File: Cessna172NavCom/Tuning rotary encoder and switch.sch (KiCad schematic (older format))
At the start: 7 parts, among them J3 EN11-HSM1BF20

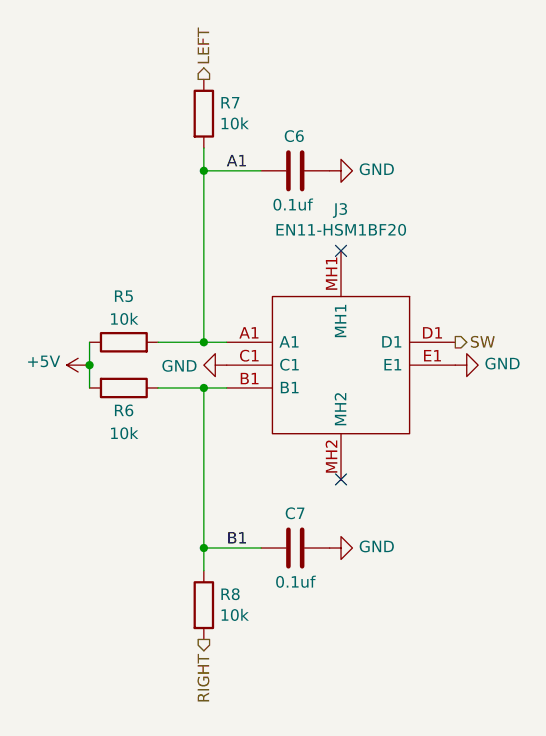
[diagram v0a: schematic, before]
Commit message: Fix courtyard overlap for routing
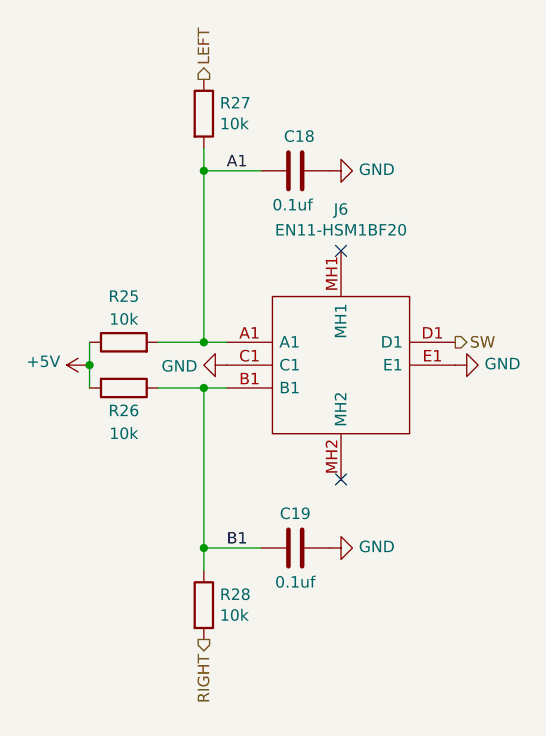
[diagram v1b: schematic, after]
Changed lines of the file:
@@
 $Descr A4 11693 8268
 encoding utf-8
-Sheet 5 15
+Sheet 14 15
 Title ""
 Date ""
@@
 AR Path="/5F71BCEB/5F5D9328" Ref="R25"  Part="1"
 AR Path="/5F71BCF7/5F5D9328" Ref="R29"  Part="1"
-F 0 "R5" V 5450 3850 50  0000 C CNN
+F 0 "R25" V 5450 3850 50  0000 C CNN
 F 1 "10k" V 5350 3850 50  0000 C CNN
 F 2 "Resistor_SMD:R_0805_2012Metric_Pad1.15x1.40mm_HandSolder" V 5180 3850 50  0001 C CNN
@@
 AR Path="/5F71BCEB/5F5D932E" Ref="R26"  Part="1"
 AR Path="/5F71BCF7/5F5D932E" Ref="R30"  Part="1"
-F 0 "R6" V 5350 4050 50  0000 C CNN
+F 0 "R26" V 5350 4050 50  0000 C CNN
 F 1 "10k" V 5450 4050 50  0000 C CNN
 F 2 "Resistor_SMD:R_0805_2012Metric_Pad1.15x1.40mm_HandSolder" V 5180 4050 50  0001 C CNN
@@
 AR Path="/5F71BCEB/5F5D9337" Ref="C19"  Part="1"
 AR Path="/5F71BCF7/5F5D9337" Ref="C21"  Part="1"
-F 0 "C7" V 6150 4750 50  0000 C CNN
+F 0 "C19" V 6150 4750 50  0000 C CNN
 F 1 "0.1uf" V 5850 4750 50  0000 C CNN
 F 2 "Capacitor_SMD:C_0805_2012Metric_Pad1.15x1.40mm_HandSolder" H 6038 4600 50  0001 C CNN
@@
 AR Path="/5F71BCEB/5F5D933D" Ref="C18"  Part="1"
 AR Path="/5F71BCF7/5F5D933D" Ref="C20"  Part="1"
-F 0 "C6" V 5850 3050 50  0000 L CNN
+F 0 "C18" V 5850 3050 50  0000 L CNN
 F 1 "0.1uf" V 6150 3000 50  0000 L CNN
 F 2 "Capacitor_SMD:C_0805_2012Metric_Pad1.15x1.40mm_HandSolder" H 6038 2950 50  0001 C CNN
@@
 AR Path="/5F71BCEB/5F5D934C" Ref="R28"  Part="1"
 AR Path="/5F71BCF7/5F5D934C" Ref="R32"  Part="1"
-F 0 "R8" H 5670 5046 50  0000 L CNN
+F 0 "R28" H 5670 5046 50  0000 L CNN
 F 1 "10k" H 5670 4955 50  0000 L CNN
 F 2 "Resistor_SMD:R_0805_2012Metric_Pad1.15x1.40mm_HandSolder" V 5530 5000 50  0001 C CNN
@@
 AR Path="/5F71BCEB/5F5D935D" Ref="R27"  Part="1"
 AR Path="/5F71BCF7/5F5D935D" Ref="R31"  Part="1"
-F 0 "R7" H 5670 2896 50  0000 L CNN
+F 0 "R27" H 5670 2896 50  0000 L CNN
 F 1 "10k" H 5670 2805 50  0000 L CNN
 F 2 "Resistor_SMD:R_0805_2012Metric_Pad1.15x1.40mm_HandSolder" V 5530 2850 50  0001 C CNN
@@
 AR Path="/5F71BCEB/5F66C873" Ref="J6"  Part="1"
 AR Path="/5F71BCF7/5F66C873" Ref="J7"  Part="1"
-F 0 "J3" V 6019 3450 50  0000 C CNN
+F 0 "J6" V 6019 3450 50  0000 C CNN
 F 1 "EN11-HSM1BF20" V 6110 3450 50  0000 C CNN
 F 2 "SamacSys_Parts:EN11HSM1BF20" H 7050 3750 50  0001 L CNN

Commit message: Fully routed!!!
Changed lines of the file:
@@
 $Descr A4 11693 8268
 encoding utf-8
-Sheet 14 15
+Sheet 15 15
 Title ""
 Date ""
@@
 AR Path="/5F71BCEB/5F5D9328" Ref="R25"  Part="1"
 AR Path="/5F71BCF7/5F5D9328" Ref="R29"  Part="1"
-F 0 "R25" V 5450 3850 50  0000 C CNN
+F 0 "R29" V 5450 3850 50  0000 C CNN
 F 1 "10k" V 5350 3850 50  0000 C CNN
 F 2 "Resistor_SMD:R_0805_2012Metric_Pad1.15x1.40mm_HandSolder" V 5180 3850 50  0001 C CNN
@@
 AR Path="/5F71BCEB/5F5D932E" Ref="R26"  Part="1"
 AR Path="/5F71BCF7/5F5D932E" Ref="R30"  Part="1"
-F 0 "R26" V 5350 4050 50  0000 C CNN
+F 0 "R30" V 5350 4050 50  0000 C CNN
 F 1 "10k" V 5450 4050 50  0000 C CNN
 F 2 "Resistor_SMD:R_0805_2012Metric_Pad1.15x1.40mm_HandSolder" V 5180 4050 50  0001 C CNN
@@
 AR Path="/5F71BCEB/5F5D9337" Ref="C19"  Part="1"
 AR Path="/5F71BCF7/5F5D9337" Ref="C21"  Part="1"
-F 0 "C19" V 6150 4750 50  0000 C CNN
+F 0 "C21" V 6150 4750 50  0000 C CNN
 F 1 "0.1uf" V 5850 4750 50  0000 C CNN
 F 2 "Capacitor_SMD:C_0805_2012Metric_Pad1.15x1.40mm_HandSolder" H 6038 4600 50  0001 C CNN
@@
 AR Path="/5F71BCEB/5F5D933D" Ref="C18"  Part="1"
 AR Path="/5F71BCF7/5F5D933D" Ref="C20"  Part="1"
-F 0 "C18" V 5850 3050 50  0000 L CNN
+F 0 "C20" V 5850 3050 50  0000 L CNN
 F 1 "0.1uf" V 6150 3000 50  0000 L CNN
 F 2 "Capacitor_SMD:C_0805_2012Metric_Pad1.15x1.40mm_HandSolder" H 6038 2950 50  0001 C CNN
@@
 AR Path="/5F71BCEB/5F5D934C" Ref="R28"  Part="1"
 AR Path="/5F71BCF7/5F5D934C" Ref="R32"  Part="1"
-F 0 "R28" H 5670 5046 50  0000 L CNN
+F 0 "R32" H 5670 5046 50  0000 L CNN
 F 1 "10k" H 5670 4955 50  0000 L CNN
 F 2 "Resistor_SMD:R_0805_2012Metric_Pad1.15x1.40mm_HandSolder" V 5530 5000 50  0001 C CNN
@@
 AR Path="/5F71BCEB/5F5D935D" Ref="R27"  Part="1"
 AR Path="/5F71BCF7/5F5D935D" Ref="R31"  Part="1"
-F 0 "R27" H 5670 2896 50  0000 L CNN
+F 0 "R31" H 5670 2896 50  0000 L CNN
 F 1 "10k" H 5670 2805 50  0000 L CNN
 F 2 "Resistor_SMD:R_0805_2012Metric_Pad1.15x1.40mm_HandSolder" V 5530 2850 50  0001 C CNN
@@
 AR Path="/5F71BCEB/5F66C873" Ref="J6"  Part="1"
 AR Path="/5F71BCF7/5F66C873" Ref="J7"  Part="1"
-F 0 "J6" V 6019 3450 50  0000 C CNN
+F 0 "J7" V 6019 3450 50  0000 C CNN
 F 1 "EN11-HSM1BF20" V 6110 3450 50  0000 C CNN
 F 2 "SamacSys_Parts:EN11HSM1BF20" H 7050 3750 50  0001 L CNN

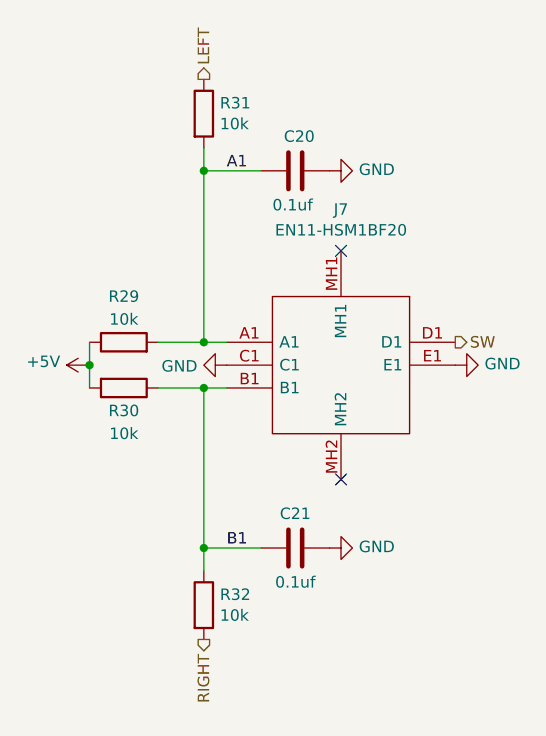
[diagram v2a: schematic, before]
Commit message: Remove unnecessary items, rename some of the nets
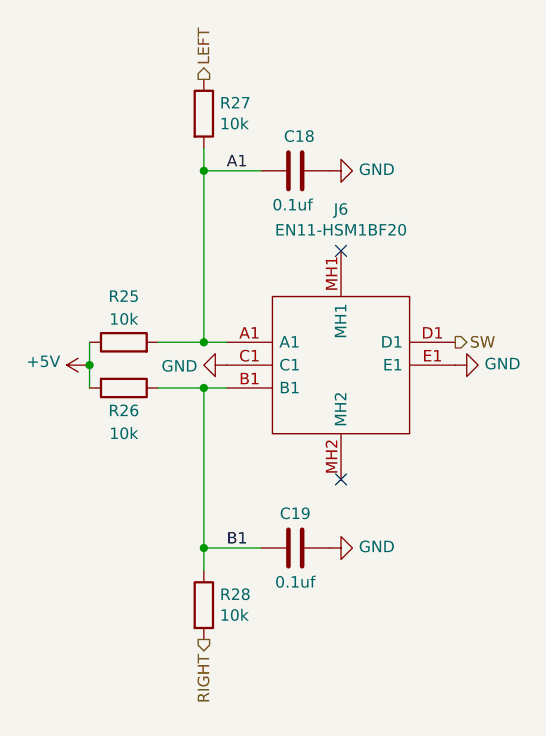
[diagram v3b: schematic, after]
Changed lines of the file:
@@
 $Descr A4 11693 8268
 encoding utf-8
-Sheet 15 15
+Sheet 13 13
 Title ""
 Date ""
@@
 AR Path="/5F71BCEB/5F5D9328" Ref="R25"  Part="1"
 AR Path="/5F71BCF7/5F5D9328" Ref="R29"  Part="1"
-F 0 "R29" V 5450 3850 50  0000 C CNN
+F 0 "R25" V 5450 3850 50  0000 C CNN
 F 1 "10k" V 5350 3850 50  0000 C CNN
 F 2 "Resistor_SMD:R_0805_2012Metric_Pad1.15x1.40mm_HandSolder" V 5180 3850 50  0001 C CNN
@@
 AR Path="/5F71BCEB/5F5D932E" Ref="R26"  Part="1"
 AR Path="/5F71BCF7/5F5D932E" Ref="R30"  Part="1"
-F 0 "R30" V 5350 4050 50  0000 C CNN
+F 0 "R26" V 5350 4050 50  0000 C CNN
 F 1 "10k" V 5450 4050 50  0000 C CNN
 F 2 "Resistor_SMD:R_0805_2012Metric_Pad1.15x1.40mm_HandSolder" V 5180 4050 50  0001 C CNN
@@
 AR Path="/5F71BCEB/5F5D9337" Ref="C19"  Part="1"
 AR Path="/5F71BCF7/5F5D9337" Ref="C21"  Part="1"
-F 0 "C21" V 6150 4750 50  0000 C CNN
+F 0 "C19" V 6150 4750 50  0000 C CNN
 F 1 "0.1uf" V 5850 4750 50  0000 C CNN
 F 2 "Capacitor_SMD:C_0805_2012Metric_Pad1.15x1.40mm_HandSolder" H 6038 4600 50  0001 C CNN
@@
 AR Path="/5F71BCEB/5F5D933D" Ref="C18"  Part="1"
 AR Path="/5F71BCF7/5F5D933D" Ref="C20"  Part="1"
-F 0 "C20" V 5850 3050 50  0000 L CNN
+F 0 "C18" V 5850 3050 50  0000 L CNN
 F 1 "0.1uf" V 6150 3000 50  0000 L CNN
 F 2 "Capacitor_SMD:C_0805_2012Metric_Pad1.15x1.40mm_HandSolder" H 6038 2950 50  0001 C CNN
@@
 AR Path="/5F71BCEB/5F5D934C" Ref="R28"  Part="1"
 AR Path="/5F71BCF7/5F5D934C" Ref="R32"  Part="1"
-F 0 "R32" H 5670 5046 50  0000 L CNN
+F 0 "R28" H 5670 5046 50  0000 L CNN
 F 1 "10k" H 5670 4955 50  0000 L CNN
 F 2 "Resistor_SMD:R_0805_2012Metric_Pad1.15x1.40mm_HandSolder" V 5530 5000 50  0001 C CNN
@@
 AR Path="/5F71BCEB/5F5D935D" Ref="R27"  Part="1"
 AR Path="/5F71BCF7/5F5D935D" Ref="R31"  Part="1"
-F 0 "R31" H 5670 2896 50  0000 L CNN
+F 0 "R27" H 5670 2896 50  0000 L CNN
 F 1 "10k" H 5670 2805 50  0000 L CNN
 F 2 "Resistor_SMD:R_0805_2012Metric_Pad1.15x1.40mm_HandSolder" V 5530 2850 50  0001 C CNN
@@
 AR Path="/5F71BCEB/5F66C873" Ref="J6"  Part="1"
 AR Path="/5F71BCF7/5F66C873" Ref="J7"  Part="1"
-F 0 "J7" V 6019 3450 50  0000 C CNN
+F 0 "J6" V 6019 3450 50  0000 C CNN
 F 1 "EN11-HSM1BF20" V 6110 3450 50  0000 C CNN
 F 2 "SamacSys_Parts:EN11HSM1BF20" H 7050 3750 50  0001 L CNN
@@
 AR Path="/5F71BCEB/5F694C04" Ref="#PWR0157"  Part="1"
 AR Path="/5F71BCF7/5F694C04" Ref="#PWR0162"  Part="1"
-F 0 "#PWR0162" H 6150 2850 50  0001 C CNN
+F 0 "#PWR0157" H 6150 2850 50  0001 C CNN
 F 1 "GND" V 6155 2972 50  0000 R CNN
 F 2 "" H 6150 3100 50  0001 C CNN
@@
 AR Path="/5F71BCEB/5F694D67" Ref="#PWR0158"  Part="1"
 AR Path="/5F71BCF7/5F694D67" Ref="#PWR0163"  Part="1"
-F 0 "#PWR0163" H 6700 3700 50  0001 C CNN
+F 0 "#PWR0158" H 6700 3700 50  0001 C CNN
 F 1 "GND" V 6705 3822 50  0000 R CNN
 F 2 "" H 6700 3950 50  0001 C CNN
@@
 AR Path="/5F71BCEB/5F694ED6" Ref="#PWR0159"  Part="1"
 AR Path="/5F71BCF7/5F694ED6" Ref="#PWR0164"  Part="1"
-F 0 "#PWR0164" H 6150 4500 50  0001 C CNN
+F 0 "#PWR0159" H 6150 4500 50  0001 C CNN
 F 1 "GND" V 6155 4622 50  0000 R CNN
 F 2 "" H 6150 4750 50  0001 C CNN
@@
 AR Path="/5F71BCEB/5F6951CA" Ref="#PWR0160"  Part="1"
 AR Path="/5F71BCF7/5F6951CA" Ref="#PWR0165"  Part="1"
-F 0 "#PWR0165" H 5700 3700 50  0001 C CNN
+F 0 "#PWR0160" H 5700 3700 50  0001 C CNN
 F 1 "GND" V 5705 3822 50  0000 R CNN
 F 2 "" H 5700 3950 50  0001 C CNN
@@
 AR Path="/5F71BCEB/5F695357" Ref="#PWR0161"  Part="1"
 AR Path="/5F71BCF7/5F695357" Ref="#PWR0166"  Part="1"
-F 0 "#PWR0166" H 5100 3800 50  0001 C CNN
+F 0 "#PWR0161" H 5100 3800 50  0001 C CNN
 F 1 "+5V" V 5115 4078 50  0000 L CNN
 F 2 "" H 5100 3950 50  0001 C CNN

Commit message: Ready for 0805 production
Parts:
- C6, C7: value 0.1uf -> 0.01uf; LCSC (none) -> C1710
- R5, R6, R7, R8: LCSC (none) -> C17414
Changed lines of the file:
@@
 $Descr A4 11693 8268
 encoding utf-8
-Sheet 13 13
+Sheet 12 13
 Title ""
 Date ""
@@
 AR Path="/5F71BCEB/5F5D9328" Ref="R25"  Part="1"
 AR Path="/5F71BCF7/5F5D9328" Ref="R29"  Part="1"
-F 0 "R25" V 5450 3850 50  0000 C CNN
+F 0 "R21" V 5450 3850 50  0000 C CNN
 F 1 "10k" V 5350 3850 50  0000 C CNN
 F 2 "Resistor_SMD:R_0805_2012Metric_Pad1.15x1.40mm_HandSolder" V 5180 3850 50  0001 C CNN
 F 3 "~" H 5250 3850 50  0001 C CNN
+F 4 "C17414" H 5250 3850 50  0001 C CNN "LCSC"
 	1    5250 3850
 	0    -1   -1   0
@@
 AR Path="/5F71BCEB/5F5D932E" Ref="R26"  Part="1"
 AR Path="/5F71BCF7/5F5D932E" Ref="R30"  Part="1"
-F 0 "R26" V 5350 4050 50  0000 C CNN
+F 0 "R22" V 5350 4050 50  0000 C CNN
 F 1 "10k" V 5450 4050 50  0000 C CNN
 F 2 "Resistor_SMD:R_0805_2012Metric_Pad1.15x1.40mm_HandSolder" V 5180 4050 50  0001 C CNN
 F 3 "~" H 5250 4050 50  0001 C CNN
+F 4 "C17414" H 5250 4050 50  0001 C CNN "LCSC"
 	1    5250 4050
 	0    1    1    0
@@
 AR Path="/5F71BCEB/5F5D9337" Ref="C19"  Part="1"
 AR Path="/5F71BCF7/5F5D9337" Ref="C21"  Part="1"
-F 0 "C19" V 6150 4750 50  0000 C CNN
-F 1 "0.1uf" V 5850 4750 50  0000 C CNN
+F 0 "C17" V 6150 4750 50  0000 C CNN
+F 1 "0.01uf" V 5850 4750 50  0000 C CNN
 F 2 "Capacitor_SMD:C_0805_2012Metric_Pad1.15x1.40mm_HandSolder" H 6038 4600 50  0001 C CNN
 F 3 "~" H 6000 4750 50  0001 C CNN
+F 4 " C1710" H 6000 4750 50  0001 C CNN "LCSC"
 	1    6000 4750
 	0    -1   -1   0
@@
 AR Path="/5F71BCEB/5F5D933D" Ref="C18"  Part="1"
 AR Path="/5F71BCF7/5F5D933D" Ref="C20"  Part="1"
-F 0 "C18" V 5850 3050 50  0000 L CNN
-F 1 "0.1uf" V 6150 3000 50  0000 L CNN
+F 0 "C16" V 5850 3050 50  0000 L CNN
+F 1 "0.01uf" V 6150 3000 50  0000 L CNN
 F 2 "Capacitor_SMD:C_0805_2012Metric_Pad1.15x1.40mm_HandSolder" H 6038 2950 50  0001 C CNN
 F 3 "~" H 6000 3100 50  0001 C CNN
+F 4 " C1710" H 6000 3100 50  0001 C CNN "LCSC"
 	1    6000 3100
 	0    1    1    0
@@
 AR Path="/5F71BCEB/5F5D934C" Ref="R28"  Part="1"
 AR Path="/5F71BCF7/5F5D934C" Ref="R32"  Part="1"
-F 0 "R28" H 5670 5046 50  0000 L CNN
+F 0 "R24" H 5670 5046 50  0000 L CNN
 F 1 "10k" H 5670 4955 50  0000 L CNN
 F 2 "Resistor_SMD:R_0805_2012Metric_Pad1.15x1.40mm_HandSolder" V 5530 5000 50  0001 C CNN
 F 3 "~" H 5600 5000 50  0001 C CNN
+F 4 "C17414" H 5600 5000 50  0001 C CNN "LCSC"
 	1    5600 5000
 	1    0    0    -1
@@
 AR Path="/5F71BCEB/5F5D935D" Ref="R27"  Part="1"
 AR Path="/5F71BCF7/5F5D935D" Ref="R31"  Part="1"
-F 0 "R27" H 5670 2896 50  0000 L CNN
+F 0 "R23" H 5670 2896 50  0000 L CNN
 F 1 "10k" H 5670 2805 50  0000 L CNN
 F 2 "Resistor_SMD:R_0805_2012Metric_Pad1.15x1.40mm_HandSolder" V 5530 2850 50  0001 C CNN
 F 3 "~" H 5600 2850 50  0001 C CNN
+F 4 "C17414" H 5600 2850 50  0001 C CNN "LCSC"
 	1    5600 2850
 	1    0    0    -1
@@
 AR Path="/5F71BCEB/5F66C873" Ref="J6"  Part="1"
 AR Path="/5F71BCF7/5F66C873" Ref="J7"  Part="1"
-F 0 "J6" V 6019 3450 50  0000 C CNN
+F 0 "J1" V 6019 3450 50  0000 C CNN
 F 1 "EN11-HSM1BF20" V 6110 3450 50  0000 C CNN
 F 2 "SamacSys_Parts:EN11HSM1BF20" H 7050 3750 50  0001 L CNN
